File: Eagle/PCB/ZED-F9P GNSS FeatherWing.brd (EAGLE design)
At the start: 50.8 x 22.9 mm, 41 parts, among them U1 ZED-F9P_ZED-F9P, U2 SPX3819-3.3, X1 SMA-142-0711-821/826

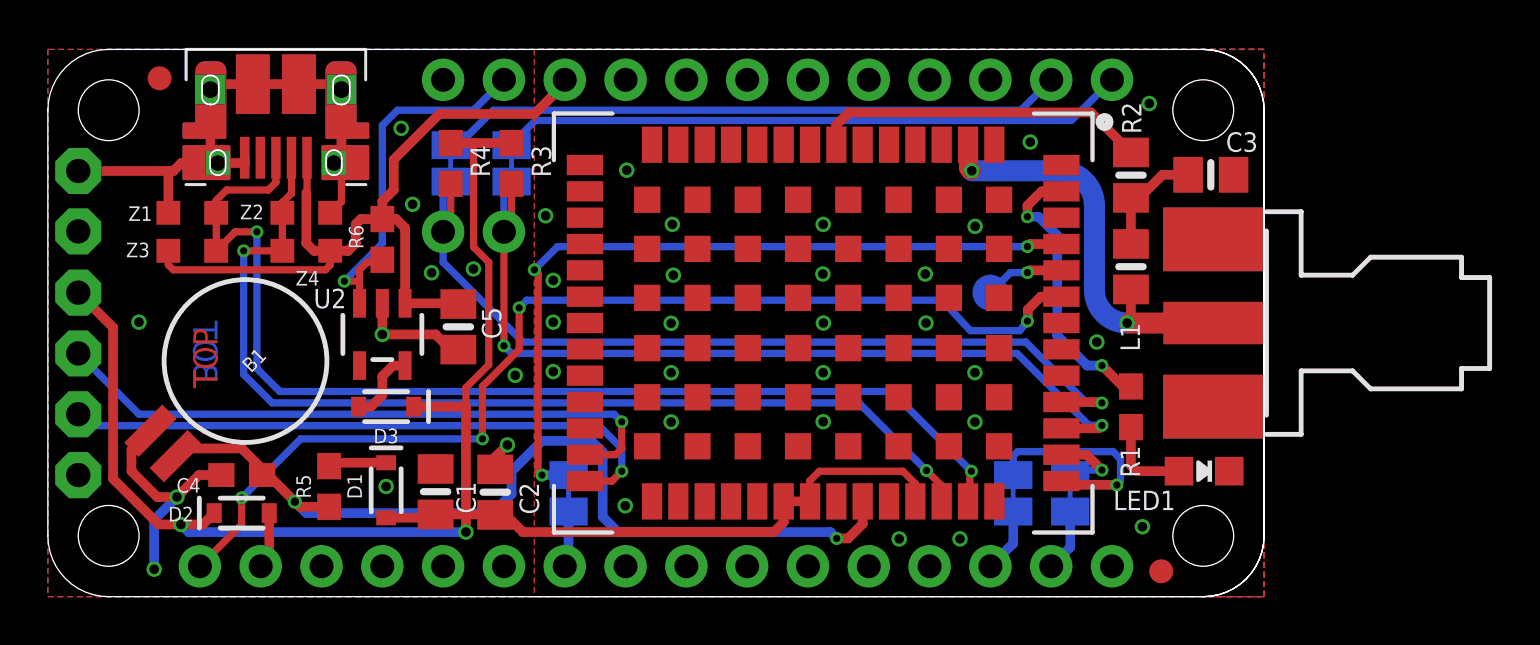
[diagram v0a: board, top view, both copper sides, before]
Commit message: Updated the power circuit
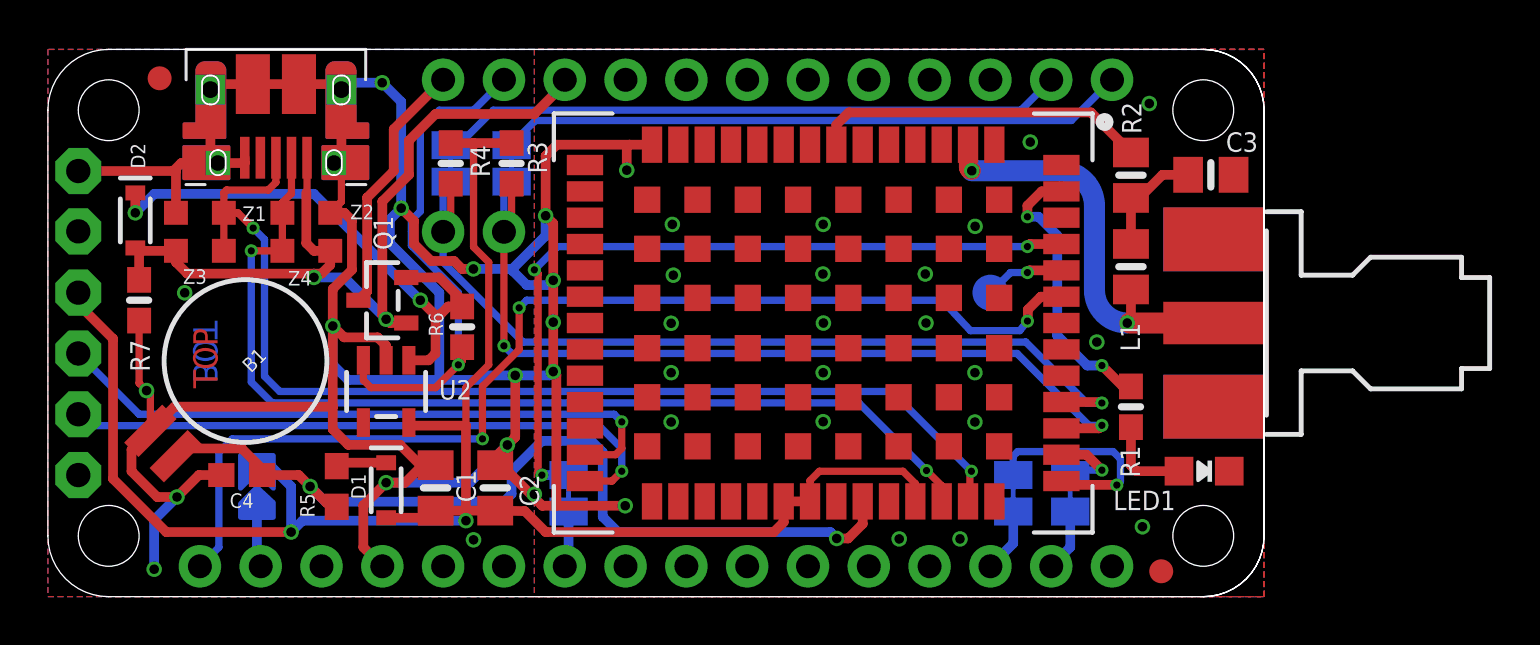
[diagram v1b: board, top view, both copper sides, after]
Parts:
- removed C5: 10µF, microbuilder:0805-NO
- removed D3: 0.5A/40V/420mV, SparkFun-DiscreteSemi:SOD-323
- added 3.3V: (no value), microbuilder:SOLDERJUMPER_ARROW_NOPASTE
- added Q1: DMG2305, microbuilder:SOT23-R
- added R7: 100K, microbuilder:0603-NO
- moved D2 13.0 mm to (3.65, 15.7), turned to 270 degrees
- moved R6 4.94 mm to (17.3, 11.3)
- moved U2 2.39 mm to (14.1, 8.57)
- moved Z1 0.32 mm to (6.35, 16.0)
- moved Z3 0.32 mm to (6.35, 14.4)
- moved R5 0.32 mm to (12.1, 4.60)
- moved C2 0.18 mm to (18.7, 4.54)
- moved C1 0.16 mm to (16.2, 4.54)
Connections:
- removed net OUT: D3.A, U2.5
- new net N$10: D2.C, Q1.2, R6.1, U2.1
- new net VBAT: MS1.28, Q1.3
- net 3.3V: now also 3.3V.2, U2.5; no longer D2.C, D3.C
- net 3V: now also 3.3V.1; no longer D2.A
- net GND: now also R7.1; no longer C5.2
- net VBUS: now also D2.A, Q1.1, R7.2; no longer C5.1, R6.1, U2.1
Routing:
- net GND: track 39.7 -> 145.8 mm, vias 38 -> 40
- net N$10: track 0.00 -> 22.9 mm, vias 0 -> 2
- net VBAT: track 0.00 -> 10.7 mm
- net EN: track 16.2 -> 21.3 mm
- net OUT: track 3.12 -> 0.00 mm
- net 3.3V: track 72.8 -> 75.0 mm
- net VBUS: track 33.8 -> 36.0 mm, vias 0 -> 2
- net GRESET: track 45.0 -> 46.7 mm, vias 4 -> 3

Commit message: Ready for manufacture
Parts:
- renumbered LED1 to PPS
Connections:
- net GRESET renamed !RESET
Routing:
- net GND: track 145.8 -> 156.3 mm, vias 40 -> 41
- net VBUS: track 36.0 -> 36.5 mm
